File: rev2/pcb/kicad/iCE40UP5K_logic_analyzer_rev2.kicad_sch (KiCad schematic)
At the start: 140 parts, among them IC1 ICE40UP5K-SG48I, IC2 MIC5504-3.3YM5-TR, IC3 MIC5504-1.2YM5-TR, IC4 FT2232HL-TRAY, IC5 W25Q40CLSNIG, IC6 SN74LVC14ADBRE4, IC7 SN74LVC14ADBRE4, IC8 SN74LVC14ADBRE4, J1 USB B Female Connector, J2 61300611121, J3 61202021621, Y1 830208214809

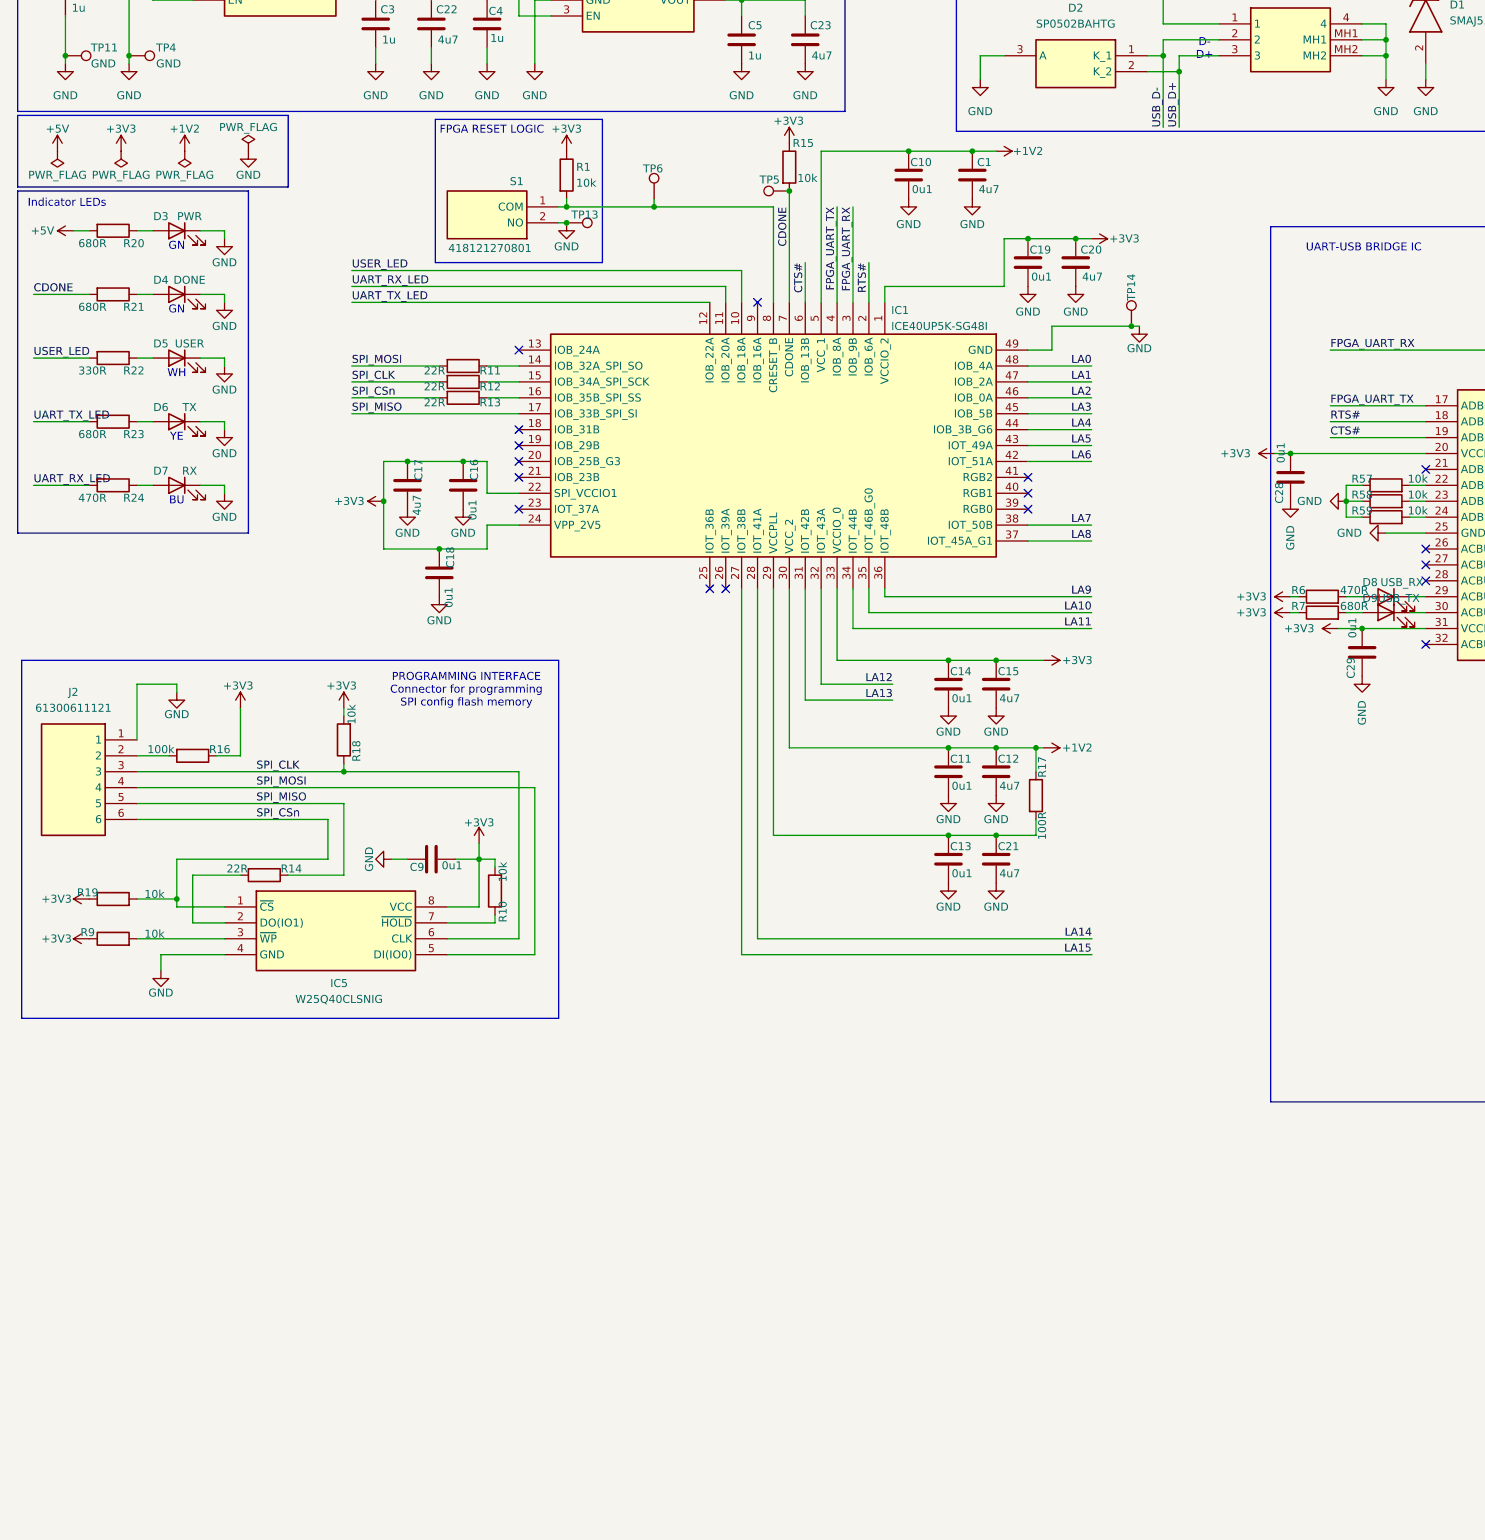
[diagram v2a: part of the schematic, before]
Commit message: Added FPGA DEBUG HEADER to schematic. top.vhd and pcf files also updated.
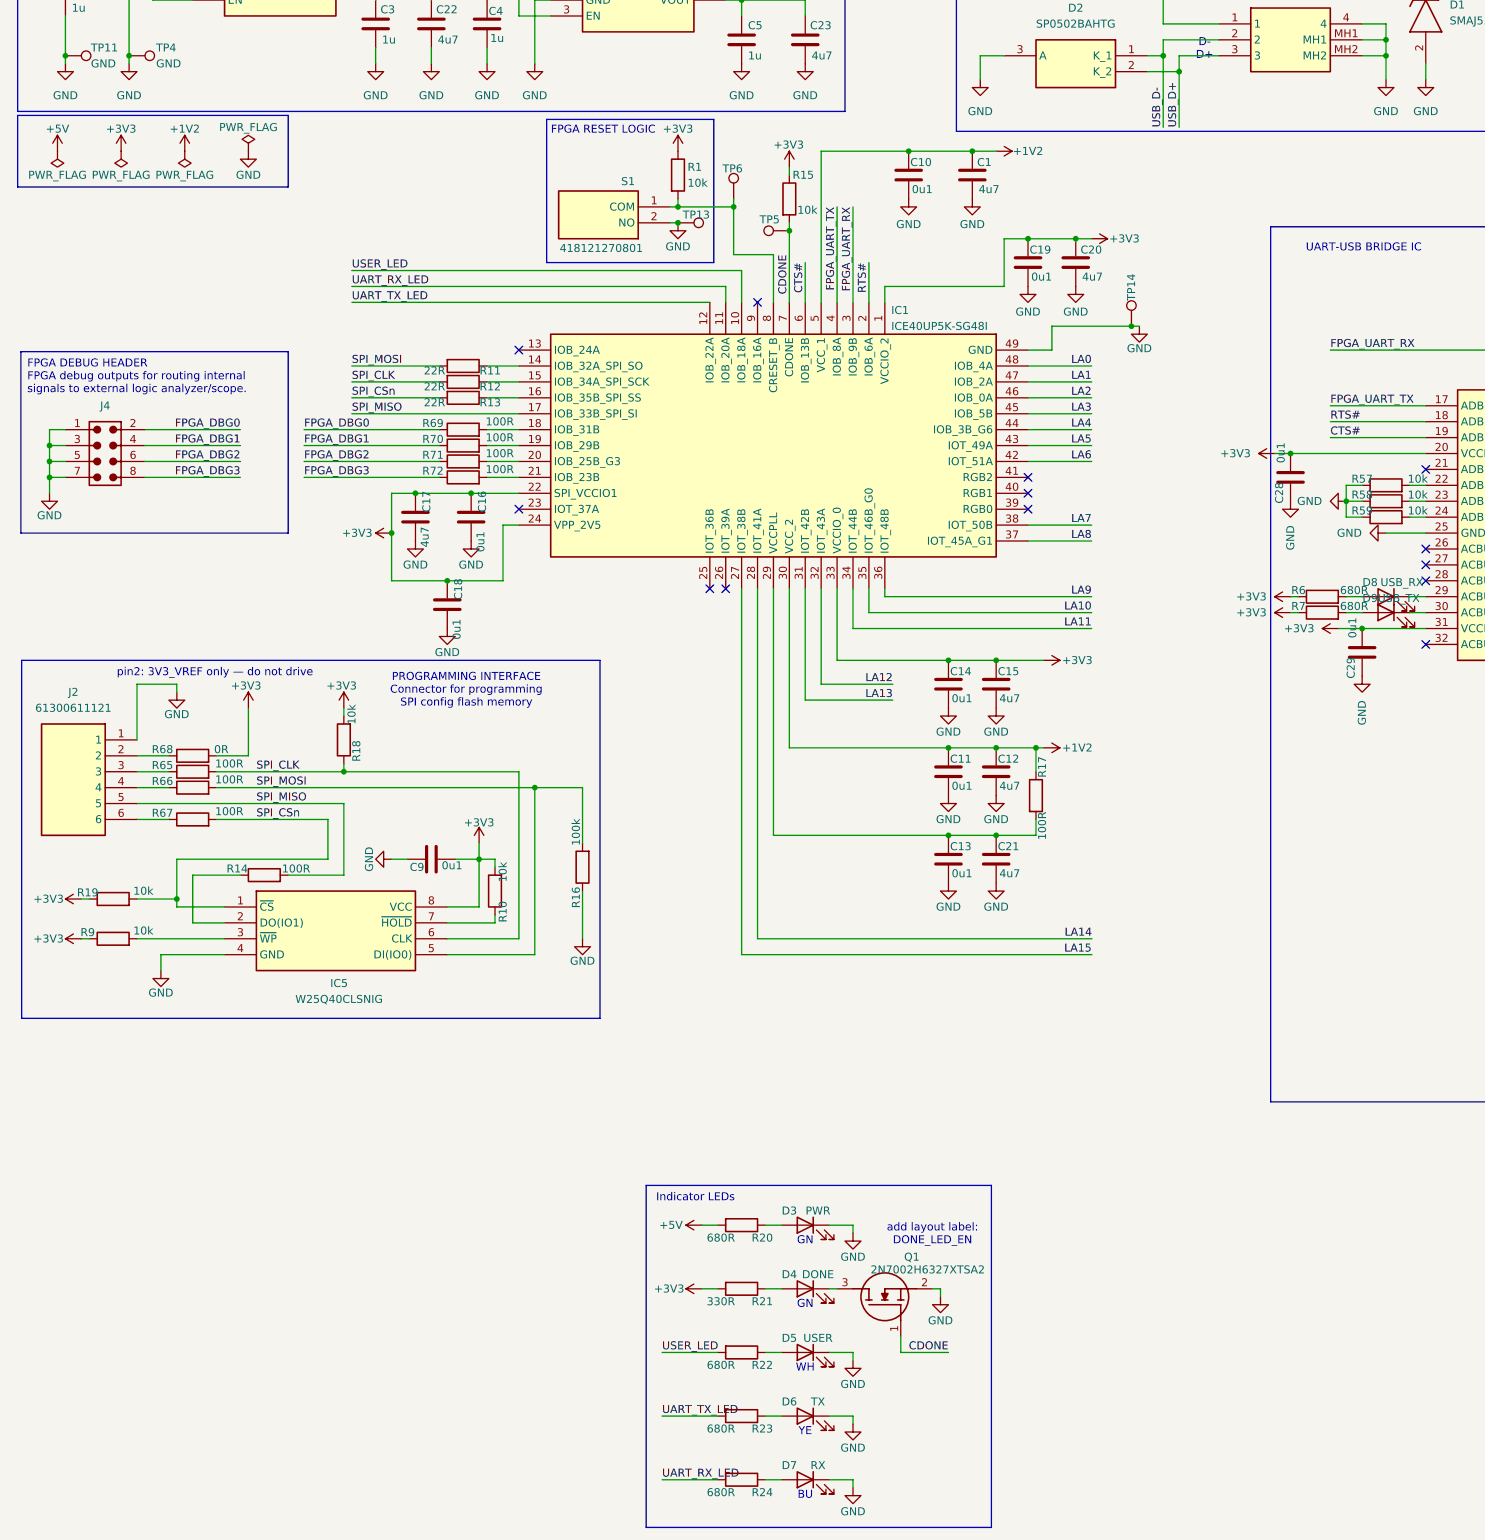
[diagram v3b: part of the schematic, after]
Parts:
- added J4: 61300821121, Connector_THT_Wurth:J_Wurth_WR-PHD_61300821121, symbol 8_pin_2x4_61300821121:61300821121
- added Q1: 2N7002H6327XTSA2, SOT95P240X110-3N, symbol NMOS_2N7002H6327XTSA2:2N7002H6327XTSA2
- added R65, R66, R67, R69, R70, R71, R72: 100R, Resistor_SMD:R_0603_1608Metric, symbol Device:R
- added R68: 0R, Resistor_SMD:R_0603_1608Metric, symbol Device:R
- R14: value 22R -> 100R
- R21: value 680R -> 330R
- R22: value 330R -> 680R
- R24, R6: value 470R -> 680R
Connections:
- net +3V3: now also R21.2, R68.2; no longer R16.1
- net CDONE: now also Q1.1 (G); no longer R21.2
- net GND: now also R16.1, J4.1, J4.3, J4.5, J4.7, Q1.2 (S); no longer D4.1 (K)
- net SPI_CLK: now also R65.2; no longer J2.3
- net SPI_CSn: now also R67.2; no longer J2.6
- net SPI_MISO: now also R14.2; no longer R14.1
- net SPI_MOSI: now also R16.2, R66.2; no longer J2.4
- net at IC1.18 (IOB_31B): now also R69.2
- net at IC1.19 (IOB_29B): now also R70.2
- net at IC1.20 (IOB_25B_G3): now also R71.2
- net at IC1.21 (IOB_23B): now also R72.2
- net at J2.2: now also R68.1; no longer R16.2
- net at IC5.2 (DO(IO1)): now also R14.1; no longer R14.2
- new net: J2.4, R66.1
- new net: J2.3, R65.1
- new net: D4.1 (K), Q1.3 (D)
- new net: J2.6, R67.1
- new net FPGA_DBG0: J4.2, R69.1
- new net FPGA_DBG1: J4.4, R70.1
- new net FPGA_DBG2: J4.6, R71.1
- new net FPGA_DBG3: J4.8, R72.1
- no-connect marks 33 -> 29
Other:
- note added: "FPGA DEBUG HEADER FPGA debug outputs for routing internal signals to external logic analyzer/scope."
- note added: "add layout label: DONE_LED_EN"
- note added: "pin2: 3V3_VREF only — do not drive"
- moved on the sheet: C16, C17, C18, D3, D4, D5, D6, D7, R1, R14, R15, R16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

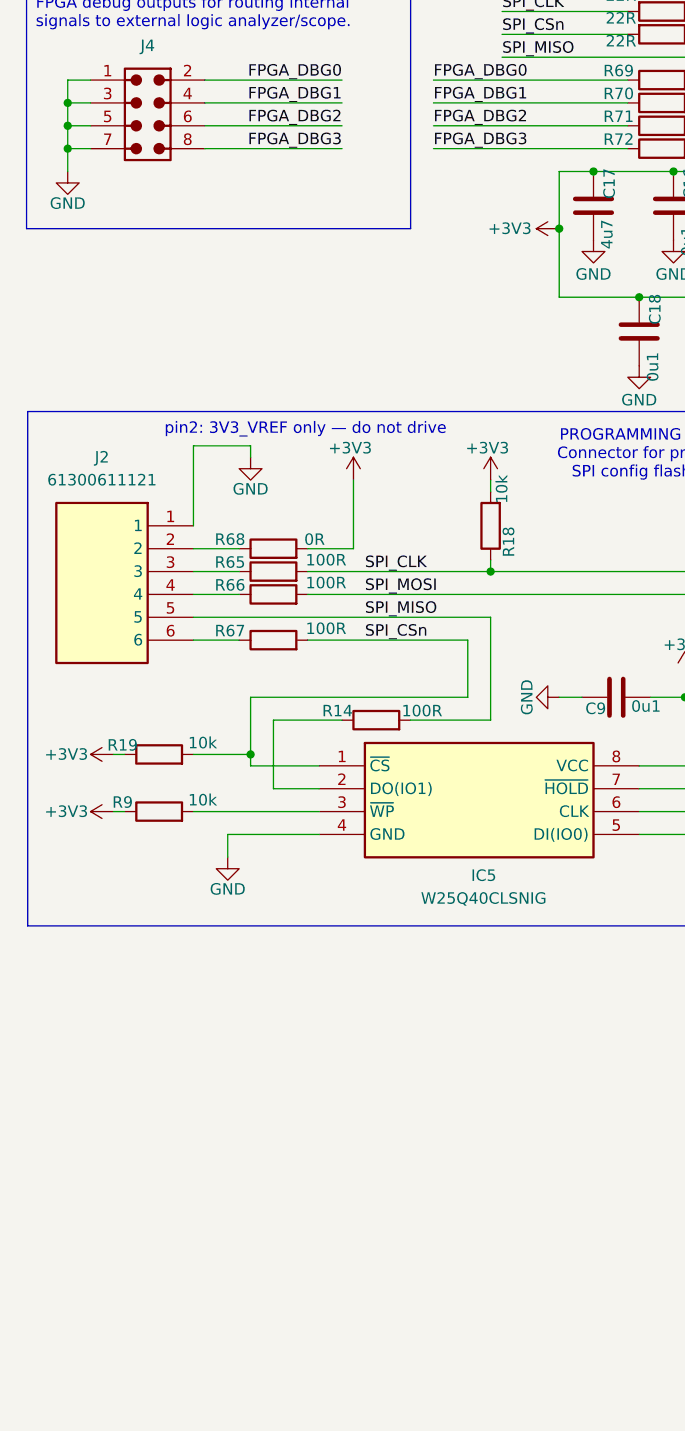
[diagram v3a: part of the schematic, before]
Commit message: Added UART PROBE HEADER to schematic.
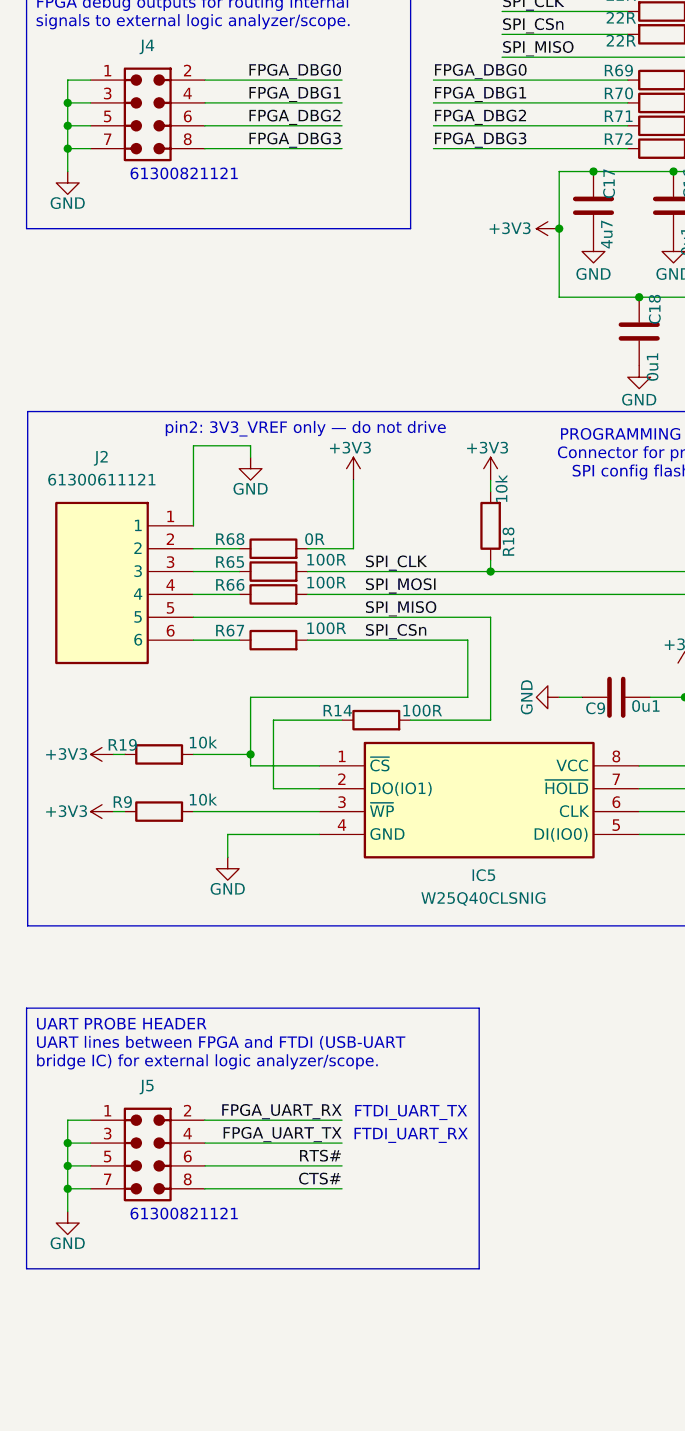
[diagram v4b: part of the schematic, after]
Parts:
- added J5: 61300821121, Connector_THT_Wurth:J_Wurth_WR-PHD_61300821121, symbol 8_pin_2x4_61300821121:61300821121
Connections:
- net CTS#: now also J5.8
- net FPGA_UART_RX: now also J5.2
- net FPGA_UART_TX: now also J5.4
- net GND: now also J5.1, J5.3, J5.5, J5.7
- net RTS#: now also J5.6
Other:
- note added: "61300821121"
- note added: "FTDI_UART_RX"
- note added: "FTDI_UART_TX"
- note added: "UART PROBE HEADER UART lines between FPGA and FTDI (USB-UART bridge IC) for external logic analyzer/scope."
